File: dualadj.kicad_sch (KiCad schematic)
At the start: 13 parts, among them J7 Conn_01x02_Female, J8 Conn_01x08_Female, J9 Conn_01x02_Female, U10 LM317L_TO92, U11 LM337L_TO92

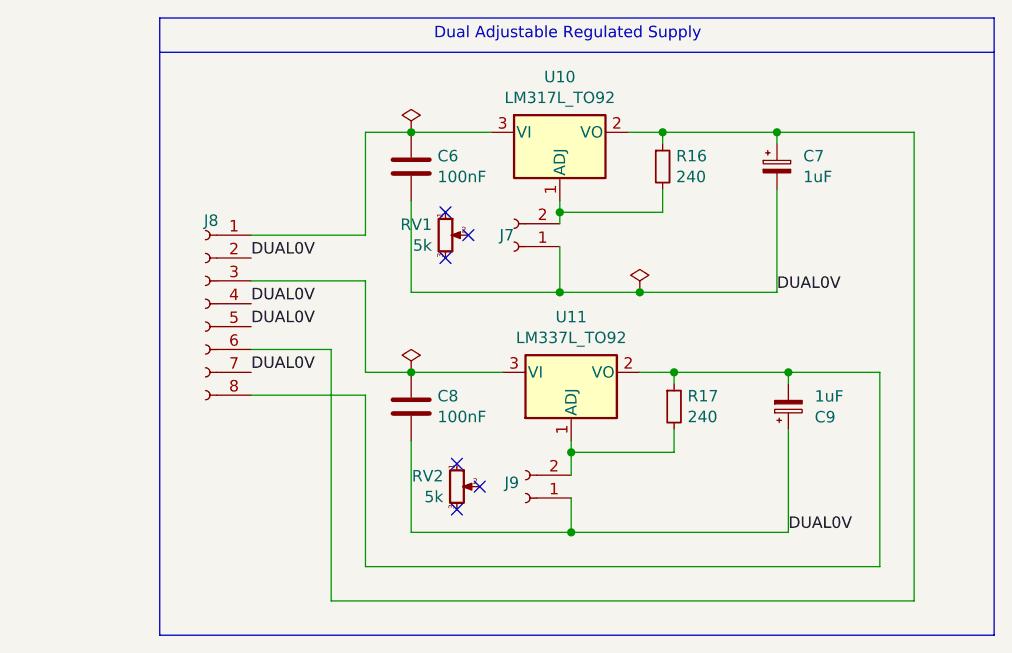
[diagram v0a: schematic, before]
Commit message: sorting out earths and making measure mux board
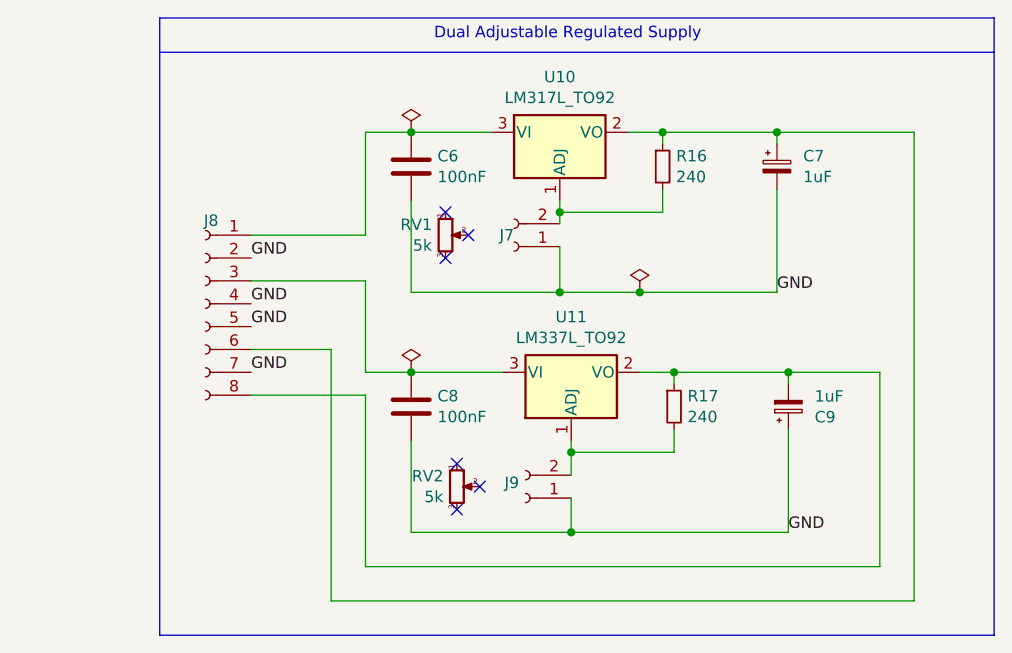
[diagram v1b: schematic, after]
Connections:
- net DUAL0V renamed GND
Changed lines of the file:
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@@
+    (stroke (width 0) (type default) (color 0 0 0 0))
+  )
+  (wire (pts (xy 143.51 116.84) (xy 167.64 116.84))
     (stroke (width 0) (type default) (color 0 0 0 0))
   )
@@
     (stroke (width 0) (type default) (color 0 0 0 0))
   )
-  (wire (pts (xy 143.51 116.84) (xy 167.64 116.84))
-    (stroke (width 0) (type default) (color 0 0 0 0))
-  )
   (wire (pts (xy 120.65 101.6) (xy 107.95 101.6))
     (stroke (width 0) (type default) (color 0 0 0 0))
@@
     (effects (font (size 1.27 1.27)) (justify left bottom))
   )
-  (label "DUAL0V" (at 167.64 116.84 0)
+  (label "GND" (at 107.95 86.36 0)
     (effects (font (size 1.27 1.27)) (justify left bottom))
   )
-  (label "DUAL0V" (at 107.95 86.36 0)
+  (label "GND" (at 166.37 90.17 0)
     (effects (font (size 1.27 1.27)) (justify left bottom))
   )
-  (label "DUAL0V" (at 107.95 93.98 0)
+  (label "GND" (at 107.95 91.44 0)
     (effects (font (size 1.27 1.27)) (justify left bottom))
   )
-  (label "DUAL0V" (at 166.37 90.17 0)
+  (label "GND" (at 107.95 93.98 0)
     (effects (font (size 1.27 1.27)) (justify left bottom))
   )
-  (label "DUAL0V" (at 107.95 99.06 0)
+  (label "GND" (at 167.64 116.84 0)
     (effects (font (size 1.27 1.27)) (justify left bottom))
   )
-  (label "DUAL0V" (at 107.95 91.44 0)
+  (label "GND" (at 107.95 99.06 0)
     (effects (font (size 1.27 1.27)) (justify left bottom))
   )

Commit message: last TH mounting board
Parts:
- C30: renamed from C6; value 100nF -> 0.1uF; footprint Capacitor_THT:C_Disc_D8.0mm_W5.0mm_P5.00mm -> Capacitor_SMD:C_0603_1608Metric
- C31: renamed from C7; footprint Capacitor_THT:C_Disc_D8.0mm_W5.0mm_P5.00mm -> Capacitor_SMD:C_1206_3216Metric
- C32: renamed from C8; value 100nF -> 0.1uF; footprint Capacitor_THT:C_Disc_D8.0mm_W5.0mm_P5.00mm -> Capacitor_SMD:C_0603_1608Metric
- C33: renamed from C9; footprint Capacitor_THT:C_Disc_D8.0mm_W5.0mm_P5.00mm -> Capacitor_SMD:C_1206_3216Metric
- R12: renamed from R16; footprint Resistor_THT:R_Axial_DIN0207_L6.3mm_D2.5mm_P5.08mm_Vertical -> Resistor_SMD:R_0603_1608Metric
- R13: renamed from R17; footprint Resistor_THT:R_Axial_DIN0207_L6.3mm_D2.5mm_P5.08mm_Vertical -> Resistor_SMD:R_0603_1608Metric
- RV1, RV2: Availability (none) -> On ORder
- U7: renamed from U10; footprint Package_TO_SOT_THT:TO-92_Inline -> Package_TO_SOT_SMD:SOT-223-3_TabPin2; Availability (none) -> on order
- U8: renamed from U11; footprint Package_TO_SOT_THT:TO-92_Inline -> Package_TO_SOT_SMD:SOT-223-3_TabPin2; Availability (none) -> on order
- renumbered J7 to J16, J8 to J17, J9 to J18
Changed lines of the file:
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@@
   (symbol (lib_id "Device:C") (at 125.73 76.2 0) (unit 1)
     (in_bom yes) (on_board yes)
-    (property "Reference" "C6" (id 0) (at 128.651 75.0316 0)
-      (effects (font (size 1.27 1.27)) (justify left))
-    )
-    (property "Value" "100nF" (id 1) (at 128.651 77.343 0)
-      (effects (font (size 1.27 1.27)) (justify left))
-    )
-    (property "Footprint" "Capacitor_THT:C_Disc_D8.0mm_W5.0mm_P5.00mm" (id 2) (at 126.6952 80.01 0)
+    (property "Reference" "C30" (id 0) (at 128.651 75.0316 0)
+      (effects (font (size 1.27 1.27)) (justify left))
+    )
+    (property "Value" "0.1uF" (id 1) (at 128.651 77.343 0)
+      (effects (font (size 1.27 1.27)) (justify left))
+    )
+    (property "Footprint" "Capacitor_SMD:C_0603_1608Metric" (id 2) (at 126.6952 80.01 0)
       (effects (font (size 1.27 1.27)) hide)
     )
@@
   (symbol (lib_id "Connector:Conn_01x02_Female") (at 138.43 113.03 180) (unit 1)
     (in_bom yes) (on_board yes) (fields_autoplaced)
-    (property "Reference" "J9" (id 0) (at 137.7188 111.3262 0)
+    (property "Reference" "J18" (id 0) (at 137.7188 111.3262 0)
       (effects (font (size 1.27 1.27)) (justify left))
     )
@@
   (symbol (lib_id "Device:C_Polarized_Small") (at 167.64 102.87 0) (mirror x) (unit 1)
     (in_bom yes) (on_board yes)
-    (property "Reference" "C9" (id 0) (at 170.561 104.0384 0)
+    (property "Reference" "C33" (id 0) (at 170.561 104.0384 0)
       (effects (font (size 1.27 1.27)) (justify left))
     )
@@
       (effects (font (size 1.27 1.27)) (justify left))
     )
-    (property "Footprint" "Capacitor_THT:C_Disc_D8.0mm_W5.0mm_P5.00mm" (id 2) (at 167.64 102.87 0)
+    (property "Footprint" "Capacitor_SMD:C_1206_3216Metric" (id 2) (at 167.64 102.87 0)
       (effects (font (size 1.27 1.27)) hide)
     )
@@
   (symbol (lib_id "Connector:Conn_01x02_Female") (at 137.16 85.09 180) (unit 1)
     (in_bom yes) (on_board yes)
-    (property "Reference" "J7" (id 0) (at 137.16 83.82 0)
+    (property "Reference" "J16" (id 0) (at 137.16 83.82 0)
       (effects (font (size 1.27 1.27)) (justify left))
     )
@@
   (symbol (lib_id "power:PWR_FLAG") (at 125.73 72.39 0) (unit 1)
     (in_bom yes) (on_board yes)
-    (property "Reference" "#FLG04" (id 0) (at 125.73 70.485 0)
+    (property "Reference" "#FLG08" (id 0) (at 125.73 70.485 0)
       (effects (font (size 1.27 1.27)) hide)
     )
@@
   (symbol (lib_id "Device:R_Small") (at 153.67 76.2 0) (unit 1)
     (in_bom yes) (on_board yes)
-    (property "Reference" "R16" (id 0) (at 155.1686 75.0316 0)
+    (property "Reference" "R12" (id 0) (at 155.1686 75.0316 0)
       (effects (font (size 1.27 1.27)) (justify left))
     )
@@
       (effects (font (size 1.27 1.27)) (justify left))
     )
-    (property "Footprint" "Resistor_THT:R_Axial_DIN0207_L6.3mm_D2.5mm_P5.08mm_Vertical" (id 2) (at 153.67 76.2 0)
+    (property "Footprint" "Resistor_SMD:R_0603_1608Metric" (id 2) (at 153.67 76.2 0)
       (effects (font (size 1.27 1.27)) hide)
     )
@@
   (symbol (lib_id "power:PWR_FLAG") (at 125.73 99.06 0) (unit 1)
     (in_bom yes) (on_board yes)
-    (property "Reference" "#FLG06" (id 0) (at 125.73 97.155 0)
+    (property "Reference" "#FLG010" (id 0) (at 125.73 97.155 0)
       (effects (font (size 1.27 1.27)) hide)
     )
@@
   (symbol (lib_id "power:PWR_FLAG") (at 151.13 90.17 0) (unit 1)
     (in_bom yes) (on_board yes)
-    (property "Reference" "#FLG05" (id 0) (at 151.13 88.265 0)
+    (property "Reference" "#FLG09" (id 0) (at 151.13 88.265 0)
       (effects (font (size 1.27 1.27)) hide)
     )
@@
   (symbol (lib_id "Regulator_Linear:LM317L_TO92") (at 142.24 72.39 0) (unit 1)
     (in_bom yes) (on_board yes)
-    (property "Reference" "U10" (id 0) (at 142.24 66.2432 0))
+    (property "Reference" "U7" (id 0) (at 142.24 66.2432 0))
     (property "Value" "LM317L_TO92" (id 1) (at 142.24 68.5546 0))
-    (property "Footprint" "Package_TO_SOT_THT:TO-92_Inline" (id 2) (at 142.24 66.675 0)
+    (property "Footprint" "Package_TO_SOT_SMD:SOT-223-3_TabPin2" (id 2) (at 142.24 66.675 0)
       (effects (font (size 1.27 1.27) italic) hide)
     )
@@
       (effects (font (size 1.27 1.27)) hide)
     )
+    (property "Availability" "on order" (id 4) (at 142.24 72.39 0)
+      (effects (font (size 1.27 1.27)) hide)
+    )
     (pin "1")
     (pin "2")
@@
       (effects (font (size 1.27 1.27)) hide)
     )
+    (property "Availability" "On ORder" (id 4) (at 130.81 111.76 0)
+      (effects (font (size 1.27 1.27)) hide)
+    )
     (pin "1")
     (pin "2")
@@
   (symbol (lib_id "Device:C") (at 125.73 102.87 0) (unit 1)
     (in_bom yes) (on_board yes)
-    (property "Reference" "C8" (id 0) (at 128.651 101.7016 0)
-      (effects (font (size 1.27 1.27)) (justify left))
-    )
-    (property "Value" "100nF" (id 1) (at 128.651 104.013 0)
-      (effects (font (size 1.27 1.27)) (justify left))
-    )
-    (property "Footprint" "Capacitor_THT:C_Disc_D8.0mm_W5.0mm_P5.00mm" (id 2) (at 126.6952 106.68 0)
+    (property "Reference" "C32" (id 0) (at 128.651 101.7016 0)
+      (effects (font (size 1.27 1.27)) (justify left))
+    )
+    (property "Value" "0.1uF" (id 1) (at 128.651 104.013 0)
+      (effects (font (size 1.27 1.27)) (justify left))
+    )
+    (property "Footprint" "Capacitor_SMD:C_0603_1608Metric" (id 2) (at 126.6952 106.68 0)
       (effects (font (size 1.27 1.27)) hide)
     )
@@
   (symbol (lib_id "Regulator_Linear:LM337L_TO92") (at 143.51 99.06 0) (mirror x) (unit 1)
     (in_bom yes) (on_board yes)
-    (property "Reference" "U11" (id 0) (at 143.51 92.9132 0))
+    (property "Reference" "U8" (id 0) (at 143.51 92.9132 0))
     (property "Value" "LM337L_TO92" (id 1) (at 143.51 95.2246 0))
-    (property "Footprint" "Package_TO_SOT_THT:TO-92_Inline" (id 2) (at 143.51 93.98 0)
+    (property "Footprint" "Package_TO_SOT_SMD:SOT-223-3_TabPin2" (id 2) (at 143.51 93.98 0)
       (effects (font (size 1.27 1.27) italic) hide)
     )
     (property "Datasheet" "http://www.ti.com/lit/ds/symlink/lm337l.pdf" (id 3) (at 143.51 99.06 0)
+      (effects (font (size 1.27 1.27)) hide)
+    )
+    (property "Availability" "on order" (id 4) (at 143.51 99.06 0)
       (effects (font (size 1.27 1.27)) hide)
     )
@@
   (symbol (lib_id "Connector:Conn_01x08_Female") (at 102.87 91.44 0) (mirror y) (unit 1)
     (in_bom yes) (on_board yes) (fields_autoplaced)
-    (property "Reference" "J8" (id 0) (at 103.505 82.2 0))
+    (property "Reference" "J17" (id 0) (at 103.505 82.2 0))
     (property "Value" "Conn_01x08_Female" (id 1) (at 103.505 103.2201 0)
       (effects (font (size 1.27 1.27)) hide)
@@
   (symbol (lib_id "Device:R_Small") (at 154.94 102.87 0) (unit 1)
     (in_bom yes) (on_board yes)
-    (property "Reference" "R17" (id 0) (at 156.4386 101.7016 0)
+    (property "Reference" "R13" (id 0) (at 156.4386 101.7016 0)
       (effects (font (size 1.27 1.27)) (justify left))
     )
@@
       (effects (font (size 1.27 1.27)) (justify left))
     )
-    (property "Footprint" "Resistor_THT:R_Axial_DIN0207_L6.3mm_D2.5mm_P5.08mm_Vertical" (id 2) (at 154.94 102.87 0)
+    (property "Footprint" "Resistor_SMD:R_0603_1608Metric" (id 2) (at 154.94 102.87 0)
       (effects (font (size 1.27 1.27)) hide)
     )
@@
   (symbol (lib_id "Device:C_Polarized_Small") (at 166.37 76.2 0) (unit 1)
     (in_bom yes) (on_board yes)
-    (property "Reference" "C7" (id 0) (at 169.291 75.0316 0)
+    (property "Reference" "C31" (id 0) (at 169.291 75.0316 0)
       (effects (font (size 1.27 1.27)) (justify left))
     )
@@
       (effects (font (size 1.27 1.27)) (justify left))
     )
-    (property "Footprint" "Capacitor_THT:C_Disc_D8.0mm_W5.0mm_P5.00mm" (id 2) (at 166.37 76.2 0)
+    (property "Footprint" "Capacitor_SMD:C_1206_3216Metric" (id 2) (at 166.37 76.2 0)
       (effects (font (size 1.27 1.27)) hide)
     )
@@
       (effects (font (size 1.27 1.27)) hide)
     )
+    (property "Availability" "On ORder" (id 4) (at 129.54 83.82 0)
+      (effects (font (size 1.27 1.27)) hide)
+    )

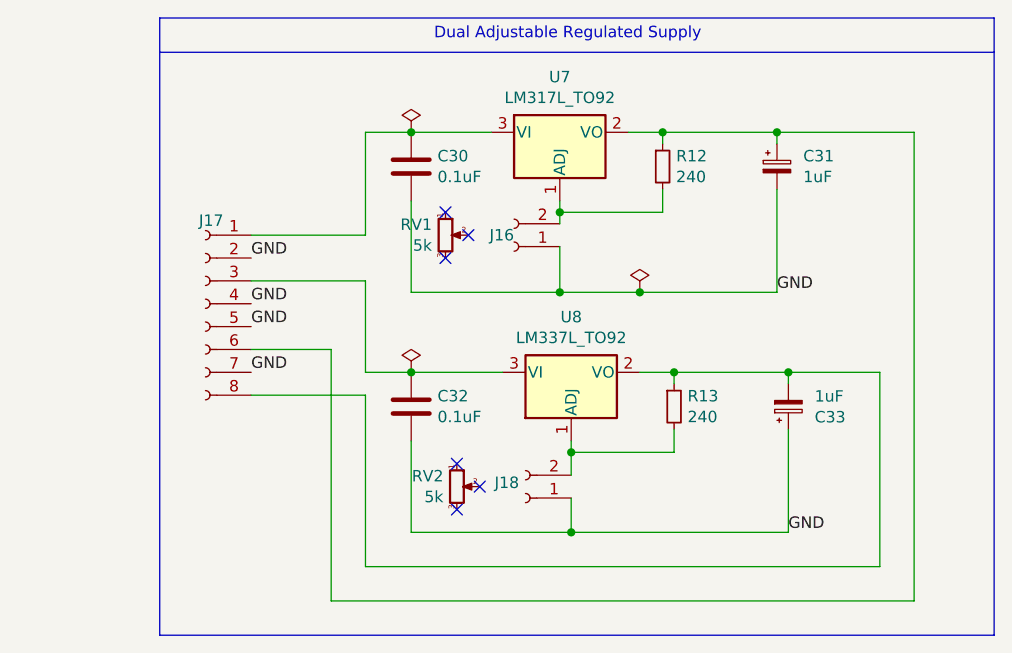
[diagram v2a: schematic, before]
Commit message: all SMD components going into boards
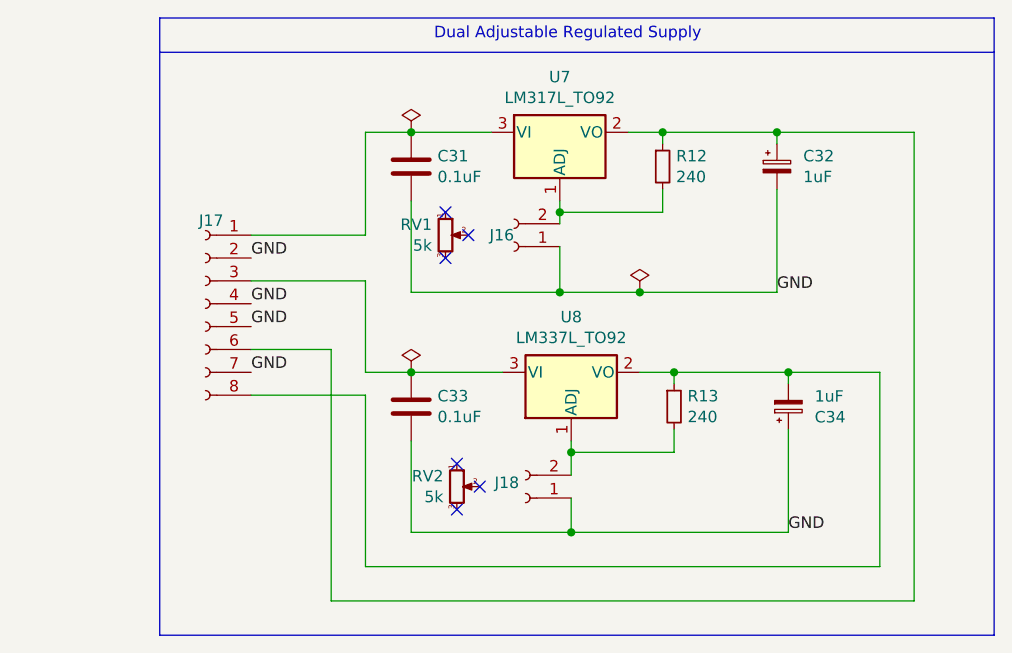
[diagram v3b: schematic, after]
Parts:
- renumbered C30 to C31, C31 to C32, C32 to C33, C33 to C34
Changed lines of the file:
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@@
   (symbol (lib_id "Device:C") (at 125.73 76.2 0) (unit 1)
     (in_bom yes) (on_board yes)
-    (property "Reference" "C30" (id 0) (at 128.651 75.0316 0)
+    (property "Reference" "C31" (id 0) (at 128.651 75.0316 0)
       (effects (font (size 1.27 1.27)) (justify left))
     )
@@
   (symbol (lib_id "Device:C_Polarized_Small") (at 167.64 102.87 0) (mirror x) (unit 1)
     (in_bom yes) (on_board yes)
-    (property "Reference" "C33" (id 0) (at 170.561 104.0384 0)
+    (property "Reference" "C34" (id 0) (at 170.561 104.0384 0)
       (effects (font (size 1.27 1.27)) (justify left))
     )
@@
   (symbol (lib_id "Device:C") (at 125.73 102.87 0) (unit 1)
     (in_bom yes) (on_board yes)
-    (property "Reference" "C32" (id 0) (at 128.651 101.7016 0)
+    (property "Reference" "C33" (id 0) (at 128.651 101.7016 0)
       (effects (font (size 1.27 1.27)) (justify left))
     )
@@
   (symbol (lib_id "Device:C_Polarized_Small") (at 166.37 76.2 0) (unit 1)
     (in_bom yes) (on_board yes)
-    (property "Reference" "C31" (id 0) (at 169.291 75.0316 0)
-      (effects (font (size 1.27 1.27)) (justify left))
-    )
+    (property "Reference" "C32" (id 0) (at 169.291 75.0316 0)
+      (effects (font (size 1.27 1.27)) (justify left))
+    )

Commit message: new board with SMD
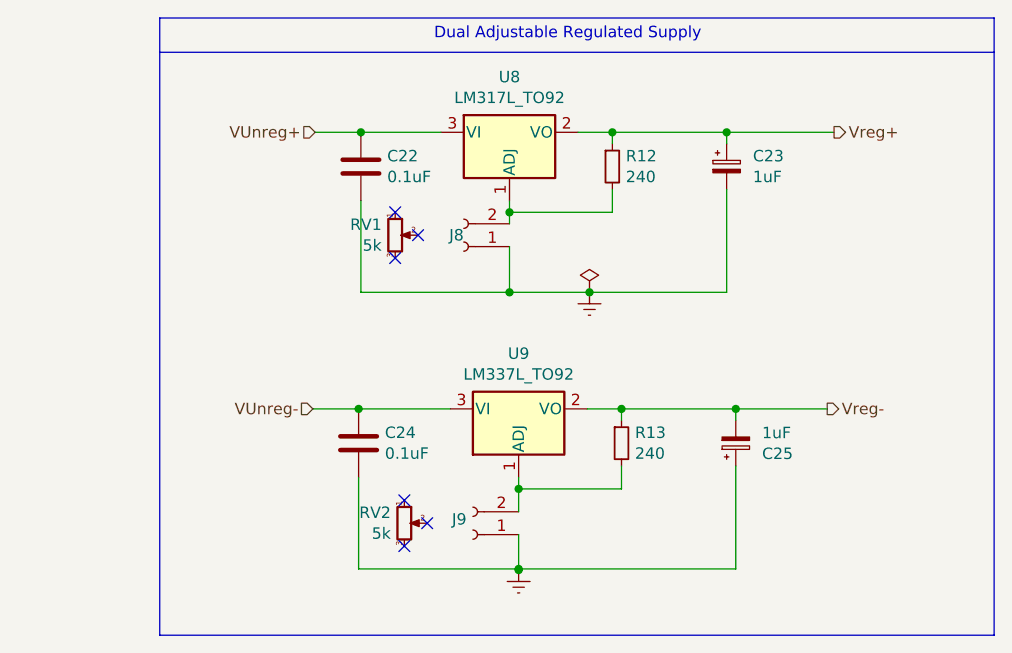
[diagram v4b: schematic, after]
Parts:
- removed J17: Conn_01x08_Female, Connector_PinHeader_2.54mm:PinHeader_1x08_P2.54mm_Vertical, symbol Connector:Conn_01x08_Female
- renumbered C31 to C22, C32 to C23, C33 to C24, C34 to C25, J16 to J8, J18 to J9, U7 to U8, U8 to U9
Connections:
- net VUnreg+: now reaches C22.1, U8.3 (VI)
- net Vreg-: now reaches C25.2, R13.1, U9.2 (VO)
- net Vreg+: now reaches C23.1, R12.1, U8.2 (VO)
- net VUnreg-: now reaches C24.1, U9.3 (VI)
- net GND: no longer names the net of C24.2, C25.1, J9.1 (Pin_1)
- net GND: no longer C22.2, C23.2, J8.1 (Pin_1)
- new net GNDREF: C22.2, C23.2, J8.1 (Pin_1)
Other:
- moved on the sheet: C22, C23, C24, C25, J8, J9, R12, R13, RV1, RV2, U8, U9

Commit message: New single board with all SMD in progress
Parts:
- C23, C25: footprint Capacitor_SMD:C_1206_3216Metric -> Capacitor_SMD:C_0603_1608Metric
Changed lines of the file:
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@@
       (effects (font (size 1.27 1.27)) (justify left))
     )
-    (property "Footprint" "Capacitor_SMD:C_1206_3216Metric" (id 2) (at 161.798 106.934 0)
+    (property "Footprint" "Capacitor_SMD:C_0603_1608Metric" (id 2) (at 161.798 106.934 0)
       (effects (font (size 1.27 1.27)) hide)
     )
@@
   (symbol (lib_id "power:GNDREF") (at 137.668 121.031 0) (unit 1)
     (in_bom yes) (on_board yes) (fields_autoplaced)
-    (property "Reference" "#PWR?" (id 0) (at 137.668 127.381 0)
+    (property "Reference" "#PWR0102" (id 0) (at 137.668 127.381 0)
       (effects (font (size 1.27 1.27)) hide)
     )
@@
   (symbol (lib_id "power:GNDREF") (at 145.542 90.17 0) (unit 1)
     (in_bom yes) (on_board yes) (fields_autoplaced)
-    (property "Reference" "#PWR?" (id 0) (at 145.542 96.52 0)
+    (property "Reference" "#PWR0103" (id 0) (at 145.542 96.52 0)
       (effects (font (size 1.27 1.27)) hide)
     )
@@
       (effects (font (size 1.27 1.27)) (justify left))
     )
-    (property "Footprint" "Capacitor_SMD:C_1206_3216Metric" (id 2) (at 160.782 76.2 0)
+    (property "Footprint" "Capacitor_SMD:C_0603_1608Metric" (id 2) (at 160.782 76.2 0)
       (effects (font (size 1.27 1.27)) hide)
     )
